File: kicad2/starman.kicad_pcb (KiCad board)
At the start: 2 copper layers, 160 x 150 mm, 104 parts, among them J1 Barrel_Jack, P1 USB_C_Plug_USB2.0, U1 ESP32-S2-MINI-1, U2 TLC5947DAP, U3 TLC5947DAP, U4 TLC5947DAP, U5 TLC5947DAP, U6 LF33_TO220, U7 LF50_TO220

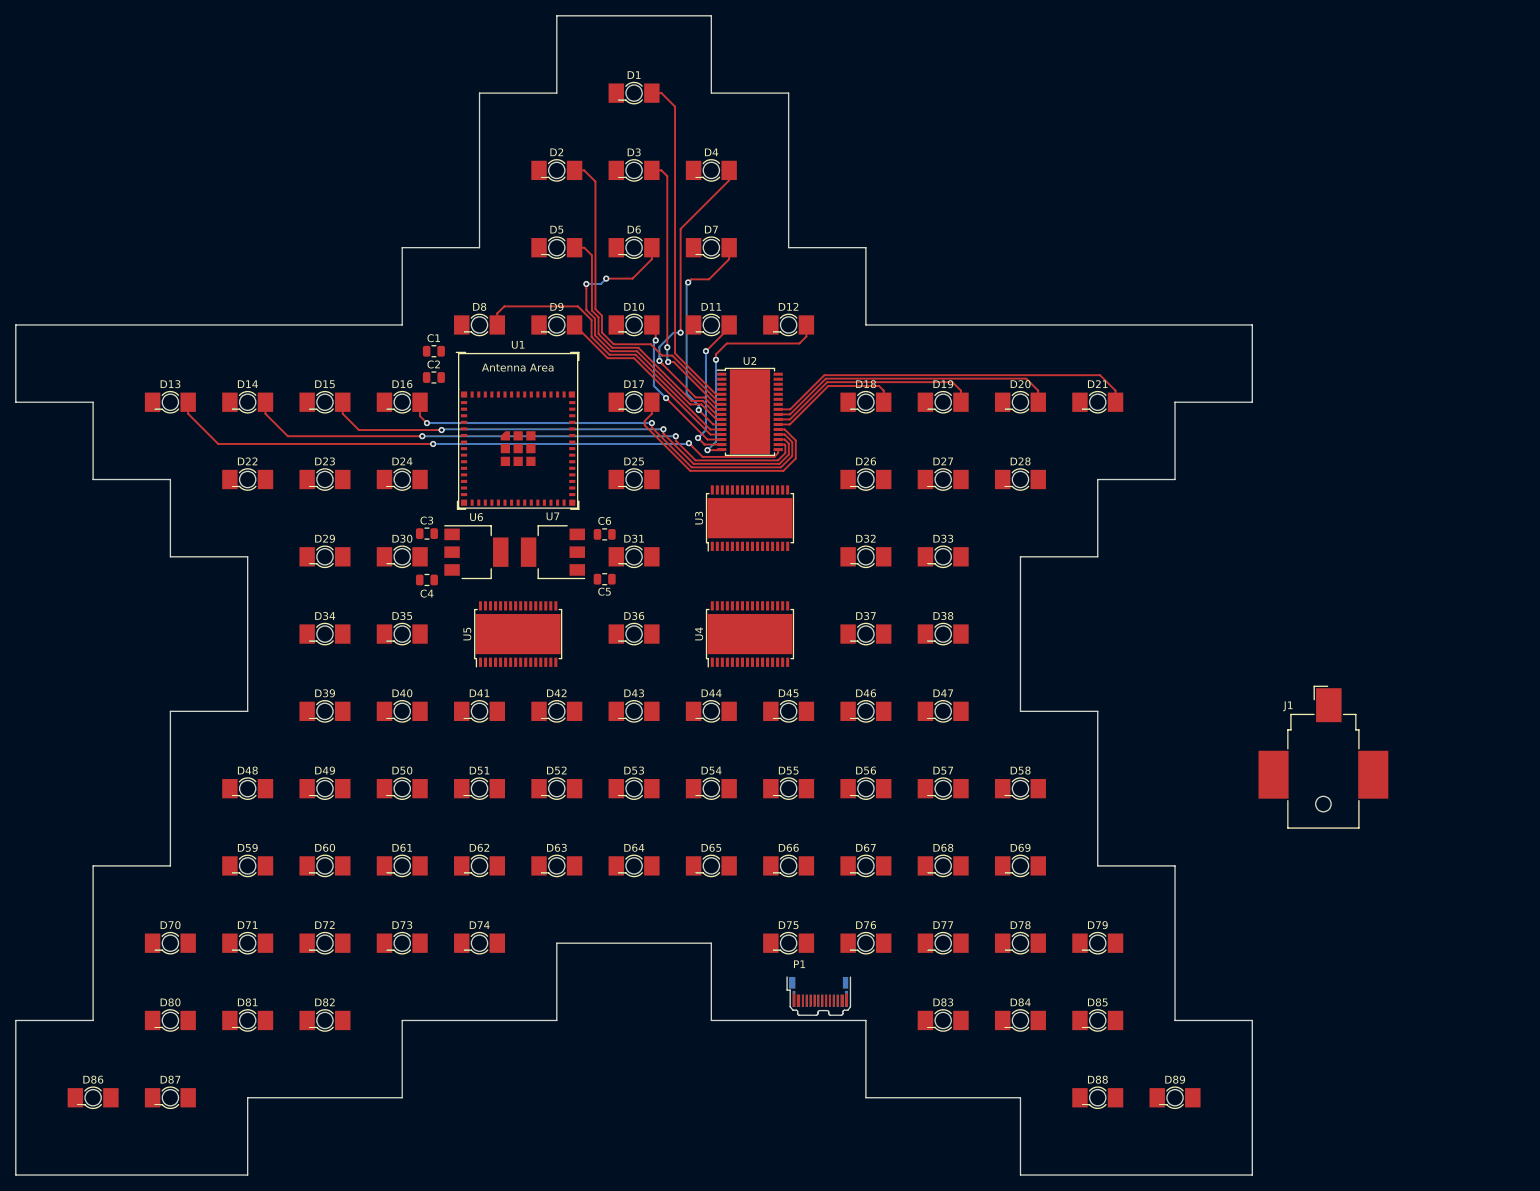
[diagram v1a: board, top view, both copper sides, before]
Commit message: Switch to PCA9959 as LED PWM driver
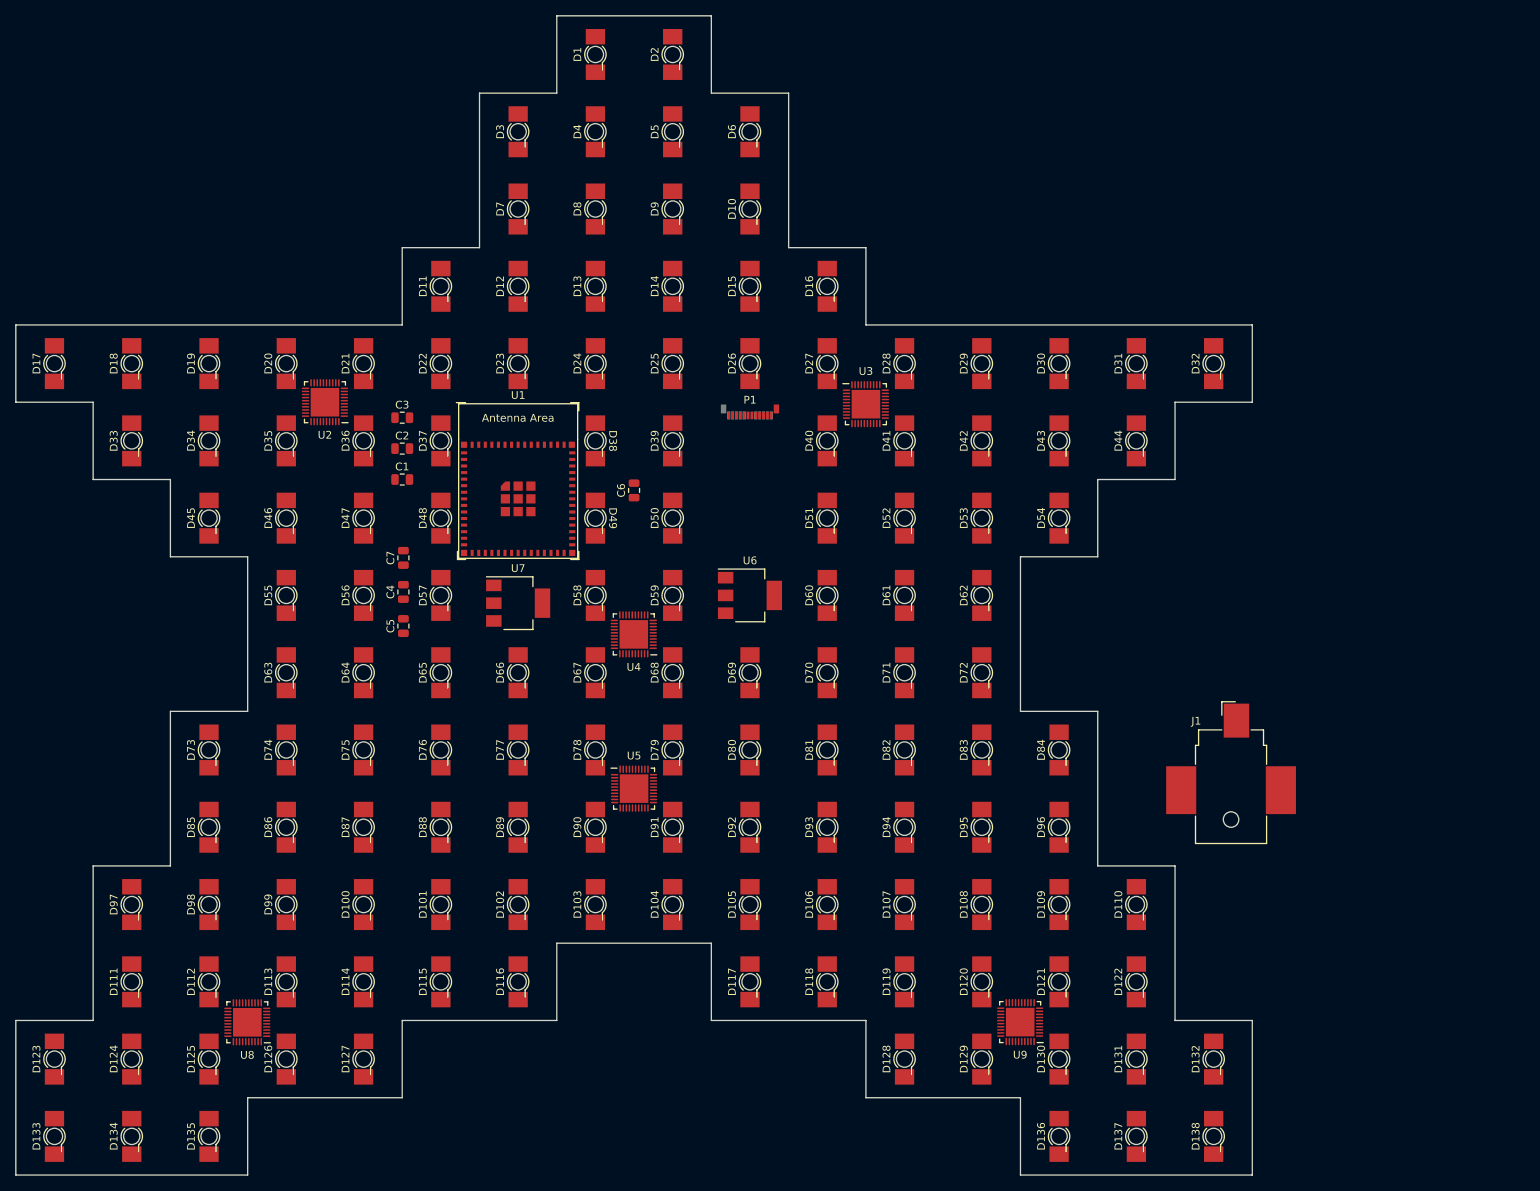
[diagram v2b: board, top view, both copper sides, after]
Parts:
- added C7: C, Capacitor_SMD:C_0805_2012Metric, F.Cu at (80.2, 100.1)
- added D100: LED, LED_SMD:LED_Osram_Lx_P47F_D2mm_ReverseMount, F.Cu at (75.0, 145.0)
- added D101: LED, LED_SMD:LED_Osram_Lx_P47F_D2mm_ReverseMount, F.Cu at (85.0, 145.0)
- added D102: LED, LED_SMD:LED_Osram_Lx_P47F_D2mm_ReverseMount, F.Cu at (95.0, 145.0)
- added D103: LED, LED_SMD:LED_Osram_Lx_P47F_D2mm_ReverseMount, F.Cu at (105.0, 145.0)
- added D104: LED, LED_SMD:LED_Osram_Lx_P47F_D2mm_ReverseMount, F.Cu at (115.0, 145.0)
- added D105: LED, LED_SMD:LED_Osram_Lx_P47F_D2mm_ReverseMount, F.Cu at (125.0, 145.0)
- added D106: LED, LED_SMD:LED_Osram_Lx_P47F_D2mm_ReverseMount, F.Cu at (135.0, 145.0)
- added D107: LED, LED_SMD:LED_Osram_Lx_P47F_D2mm_ReverseMount, F.Cu at (145.0, 145.0)
- added D108: LED, LED_SMD:LED_Osram_Lx_P47F_D2mm_ReverseMount, F.Cu at (155.0, 145.0)
- added D109: LED, LED_SMD:LED_Osram_Lx_P47F_D2mm_ReverseMount, F.Cu at (165.0, 145.0)
- added D110: LED, LED_SMD:LED_Osram_Lx_P47F_D2mm_ReverseMount, F.Cu at (175.0, 145.0)
- added D111: LED, LED_SMD:LED_Osram_Lx_P47F_D2mm_ReverseMount, F.Cu at (45.0, 155.0)
- added D112: LED, LED_SMD:LED_Osram_Lx_P47F_D2mm_ReverseMount, F.Cu at (55.0, 155.0)
- added D113: LED, LED_SMD:LED_Osram_Lx_P47F_D2mm_ReverseMount, F.Cu at (65.0, 155.0)
- added D114: LED, LED_SMD:LED_Osram_Lx_P47F_D2mm_ReverseMount, F.Cu at (75.0, 155.0)
- added D115: LED, LED_SMD:LED_Osram_Lx_P47F_D2mm_ReverseMount, F.Cu at (85.0, 155.0)
- added D116: LED, LED_SMD:LED_Osram_Lx_P47F_D2mm_ReverseMount, F.Cu at (95.0, 155.0)
- added D117: LED, LED_SMD:LED_Osram_Lx_P47F_D2mm_ReverseMount, F.Cu at (125.0, 155.0)
- added D118: LED, LED_SMD:LED_Osram_Lx_P47F_D2mm_ReverseMount, F.Cu at (135.0, 155.0)
- added D119: LED, LED_SMD:LED_Osram_Lx_P47F_D2mm_ReverseMount, F.Cu at (145.0, 155.0)
- added D120: LED, LED_SMD:LED_Osram_Lx_P47F_D2mm_ReverseMount, F.Cu at (155.0, 155.0)
- added D121: LED, LED_SMD:LED_Osram_Lx_P47F_D2mm_ReverseMount, F.Cu at (165.0, 155.0)
- added D122: LED, LED_SMD:LED_Osram_Lx_P47F_D2mm_ReverseMount, F.Cu at (175.0, 155.0)
- added D123: LED, LED_SMD:LED_Osram_Lx_P47F_D2mm_ReverseMount, F.Cu at (35.0, 165.0)
- added D124: LED, LED_SMD:LED_Osram_Lx_P47F_D2mm_ReverseMount, F.Cu at (45.0, 165.0)
- added D125: LED, LED_SMD:LED_Osram_Lx_P47F_D2mm_ReverseMount, F.Cu at (55.0, 165.0)
- added D126: LED, LED_SMD:LED_Osram_Lx_P47F_D2mm_ReverseMount, F.Cu at (65.0, 165.0)
- added D127: LED, LED_SMD:LED_Osram_Lx_P47F_D2mm_ReverseMount, F.Cu at (75.0, 165.0)
- added D128: LED, LED_SMD:LED_Osram_Lx_P47F_D2mm_ReverseMount, F.Cu at (145.0, 165.0)
- added D129: LED, LED_SMD:LED_Osram_Lx_P47F_D2mm_ReverseMount, F.Cu at (155.0, 165.0)
- added D130: LED, LED_SMD:LED_Osram_Lx_P47F_D2mm_ReverseMount, F.Cu at (165.0, 165.0)
- added D131: LED, LED_SMD:LED_Osram_Lx_P47F_D2mm_ReverseMount, F.Cu at (175.0, 165.0)
- added D132: LED, LED_SMD:LED_Osram_Lx_P47F_D2mm_ReverseMount, F.Cu at (185.0, 165.0)
- added D133: LED, LED_SMD:LED_Osram_Lx_P47F_D2mm_ReverseMount, F.Cu at (35.0, 175.0)
- added D134: LED, LED_SMD:LED_Osram_Lx_P47F_D2mm_ReverseMount, F.Cu at (45.0, 175.0)
- added D135: LED, LED_SMD:LED_Osram_Lx_P47F_D2mm_ReverseMount, F.Cu at (55.0, 175.0)
- added D136: LED, LED_SMD:LED_Osram_Lx_P47F_D2mm_ReverseMount, F.Cu at (165.0, 175.0)
- added D137: LED, LED_SMD:LED_Osram_Lx_P47F_D2mm_ReverseMount, F.Cu at (175.0, 175.0)
- added D138: LED, LED_SMD:LED_Osram_Lx_P47F_D2mm_ReverseMount, F.Cu at (185.0, 175.0)
- added D90: LED, LED_SMD:LED_Osram_Lx_P47F_D2mm_ReverseMount, F.Cu at (105.0, 135.0)
- added D91: LED, LED_SMD:LED_Osram_Lx_P47F_D2mm_ReverseMount, F.Cu at (115.0, 135.0)
- added D92: LED, LED_SMD:LED_Osram_Lx_P47F_D2mm_ReverseMount, F.Cu at (125.0, 135.0)
- added D93: LED, LED_SMD:LED_Osram_Lx_P47F_D2mm_ReverseMount, F.Cu at (135.0, 135.0)
- added D94: LED, LED_SMD:LED_Osram_Lx_P47F_D2mm_ReverseMount, F.Cu at (145.0, 135.0)
- added D95: LED, LED_SMD:LED_Osram_Lx_P47F_D2mm_ReverseMount, F.Cu at (155.0, 135.0)
- added D96: LED, LED_SMD:LED_Osram_Lx_P47F_D2mm_ReverseMount, F.Cu at (165.0, 135.0)
- added D97: LED, LED_SMD:LED_Osram_Lx_P47F_D2mm_ReverseMount, F.Cu at (45.0, 145.0)
- added D98: LED, LED_SMD:LED_Osram_Lx_P47F_D2mm_ReverseMount, F.Cu at (55.0, 145.0)
- added D99: LED, LED_SMD:LED_Osram_Lx_P47F_D2mm_ReverseMount, F.Cu at (65.0, 145.0)
- added U8: PCA9959, starman:QFN-40_EP_5x5_Pitch0.4mm, F.Cu at (60.0, 160.2)
- added U9: PCA9959, starman:QFN-40_EP_5x5_Pitch0.4mm, F.Cu at (160.0, 160.2)
- C1, C2: value C -> 10uF
- C3: value C -> 1uF
- P1: footprint Connector_USB:USB_C_Plug_JAE_DX07P024AJ1 -> Connector_USB:USB_C_Plug_Molex_105444
- U2, U3, U4, U5: value TLC5947DAP -> PCA9959; footprint Package_SO:HTSSOP-32-1EP_6.1x11mm_P0.65mm_EP5.2x11mm_Mask4.11x4.36mm -> starman:QFN-40_EP_5x5_Pitch0.4mm
- moved D85 117.7 mm to (55.0, 135.0), turned to 90 degrees
- moved D33 106.1 mm to (45.0, 85.0), turned to 90 degrees
- moved D18 95.1 mm to (45.0, 75.0), turned to 90 degrees
- moved D19 95.1 mm to (55.0, 75.0), turned to 90 degrees
- moved D20 95.1 mm to (65.0, 75.0), turned to 90 degrees
- moved D21 95.1 mm to (75.0, 75.0), turned to 90 degrees
- moved D70 91.9 mm to (135.0, 115.0), turned to 90 degrees
- moved D71 91.9 mm to (145.0, 115.0), turned to 90 degrees
- moved D72 91.9 mm to (155.0, 115.0), turned to 90 degrees
- moved D88 91.9 mm to (85.0, 135.0), turned to 90 degrees
- moved D89 91.9 mm to (95.0, 135.0), turned to 90 degrees
- moved D29 88.6 mm to (155.0, 75.0), turned to 90 degrees
- moved D30 88.6 mm to (165.0, 75.0), turned to 90 degrees
- moved D80 82.8 mm to (125.0, 125.0), turned to 90 degrees
- moved D81 82.8 mm to (135.0, 125.0), turned to 90 degrees
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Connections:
- C1 pad 1: Net-(C1-Pad1) -> GND
- C2 pad 1: Net-(C1-Pad1) -> GND
- C3 pad 2: Net-(C3-Pad2) -> +3V3
- C4 pad 2: +3V3 -> Net-(C4-Pad2)
- C5 pad 2: Net-(C3-Pad2) -> +3V3
- C6 pad 2: +5V -> Net-(C4-Pad2)
- D1 pad 1: GND -> Net-(D1-Pad1)
- D10 pad 1: GND -> Net-(D10-Pad1)
- D11 pad 1: GND -> Net-(D11-Pad1)
- D12 pad 1: GND -> Net-(D12-Pad1)
- D13 pad 1: GND -> Net-(D13-Pad1)
- D14 pad 1: GND -> Net-(D14-Pad1)
- D15 pad 1: GND -> Net-(D15-Pad1)
- D16 pad 1: GND -> Net-(D16-Pad1)
- D17 pad 1: GND -> Net-(D17-Pad1)
- D18 pad 1: GND -> Net-(D18-Pad1)
- D19 pad 1: GND -> Net-(D19-Pad1)
- D2 pad 1: GND -> Net-(D2-Pad1)
- D20 pad 1: GND -> Net-(D20-Pad1)
- D21 pad 1: GND -> Net-(D21-Pad1)
- D22 pad 1: GND -> Net-(D22-Pad1)
- D23 pad 1: GND -> Net-(D23-Pad1)
- D24 pad 1: GND -> Net-(D24-Pad1)
- D25 pad 1: GND -> Net-(D25-Pad1)
- D26 pad 1: GND -> Net-(D26-Pad1)
- D27 pad 1: GND -> Net-(D27-Pad1)
- D28 pad 1: GND -> Net-(D28-Pad1)
- D29 pad 1: GND -> Net-(D29-Pad1)
- D3 pad 1: GND -> Net-(D3-Pad1)
- D30 pad 1: GND -> Net-(D30-Pad1)
- D31 pad 1: GND -> Net-(D31-Pad1)
- D32 pad 1: GND -> Net-(D32-Pad1)
- D33 pad 1: GND -> Net-(D33-Pad1)
- D34 pad 1: GND -> Net-(D34-Pad1)
- D35 pad 1: GND -> Net-(D35-Pad1)
- D36 pad 1: GND -> Net-(D36-Pad1)
- D37 pad 1: GND -> Net-(D37-Pad1)
- D38 pad 1: GND -> Net-(D38-Pad1)
- D39 pad 1: GND -> Net-(D39-Pad1)
- D4 pad 1: GND -> Net-(D4-Pad1)
- D40 pad 1: GND -> Net-(D40-Pad1)
- D41 pad 1: GND -> Net-(D41-Pad1)
- D42 pad 1: GND -> Net-(D42-Pad1)
- D43 pad 1: GND -> Net-(D43-Pad1)
- D44 pad 1: GND -> Net-(D44-Pad1)
- D45 pad 1: GND -> Net-(D45-Pad1)
- D46 pad 1: GND -> Net-(D46-Pad1)
- D47 pad 1: GND -> Net-(D47-Pad1)
- D48 pad 1: GND -> Net-(D48-Pad1)
- D49 pad 1: GND -> Net-(D49-Pad1)
- D5 pad 1: GND -> Net-(D5-Pad1)
- D50 pad 1: GND -> Net-(D50-Pad1)
- D51 pad 1: GND -> Net-(D51-Pad1)
- D52 pad 1: GND -> Net-(D52-Pad1)
- D53 pad 1: GND -> Net-(D53-Pad1)
- D54 pad 1: GND -> Net-(D54-Pad1)
- D55 pad 1: GND -> Net-(D55-Pad1)
- D56 pad 1: GND -> Net-(D56-Pad1)
- D57 pad 1: GND -> Net-(D57-Pad1)
- D58 pad 1: GND -> Net-(D58-Pad1)
- D59 pad 1: GND -> Net-(D59-Pad1)
- D6 pad 1: GND -> Net-(D6-Pad1)
- D60 pad 1: GND -> Net-(D60-Pad1)
- D61 pad 1: GND -> Net-(D61-Pad1)
- D62 pad 1: GND -> Net-(D62-Pad1)
- D63 pad 1: GND -> Net-(D63-Pad1)
- D64 pad 1: GND -> Net-(D64-Pad1)
- D65 pad 1: GND -> Net-(D65-Pad1)
- D66 pad 1: GND -> Net-(D66-Pad1)
- D67 pad 1: GND -> Net-(D67-Pad1)
- D68 pad 1: GND -> Net-(D68-Pad1)
- D69 pad 1: GND -> Net-(D69-Pad1)
- D7 pad 1: GND -> Net-(D7-Pad1)
- D70 pad 1: GND -> Net-(D70-Pad1)
- D71 pad 1: GND -> Net-(D71-Pad1)
- D72 pad 1: GND -> Net-(D72-Pad1)
- D73 pad 1: GND -> Net-(D73-Pad1)
- D74 pad 1: GND -> Net-(D74-Pad1)
- D75 pad 1: GND -> Net-(D75-Pad1)
- D76 pad 1: GND -> Net-(D76-Pad1)
- D77 pad 1: GND -> Net-(D77-Pad1)
- D78 pad 1: GND -> Net-(D78-Pad1)
- D79 pad 1: GND -> Net-(D79-Pad1)
- D8 pad 1: GND -> Net-(D8-Pad1)
- D80 pad 1: GND -> Net-(D80-Pad1)
- D81 pad 1: GND -> Net-(D81-Pad1)
- D82 pad 1: GND -> Net-(D82-Pad1)
- D83 pad 1: GND -> Net-(D83-Pad1)
- D84 pad 1: GND -> Net-(D84-Pad1)
- D85 pad 1: GND -> Net-(D85-Pad1)
- D86 pad 1: GND -> Net-(D86-Pad1)
- D87 pad 1: GND -> Net-(D87-Pad1)
- D88 pad 1: GND -> Net-(D88-Pad1)
- D89 pad 1: GND -> Net-(D89-Pad1)
- D9 pad 1: GND -> Net-(D9-Pad1)
- J1 pad 1: Net-(C3-Pad2) -> Net-(C4-Pad2)
- P1 pad A8: (no net) -> Net-(P1-PadA8)
- P1 pad B8: (no net) -> Net-(P1-PadB8)
- U1 pad 1: Net-(C1-Pad1) -> GND
- U1 pad 2: Net-(C1-Pad1) -> GND
- U1 pad 30: Net-(C1-Pad1) -> GND
- U1 pad 42: Net-(C1-Pad1) -> GND
- U1 pad 43: Net-(C1-Pad1) -> GND
- U1 pad 46: Net-(C1-Pad1) -> GND
- U2 pad 1: GND -> Net-(U2-Pad1)
- U2 pad 10: Net-(D6-Pad2) -> Net-(U2-Pad10)
- U2 pad 11: Net-(D7-Pad2) -> Net-(U2-Pad11)
- U2 pad 12: Net-(D8-Pad2) -> Net-(U2-Pad12)
- U2 pad 13: Net-(D9-Pad2) -> Net-(D1-Pad1)
- U2 pad 14: Net-(D10-Pad2) -> Net-(D3-Pad1)
- U2 pad 15: Net-(D11-Pad2) -> Net-(D4-Pad1)
- U2 pad 16: Net-(D12-Pad2) -> Net-(D7-Pad1)
- U2 pad 17: Net-(D13-Pad2) -> Net-(D8-Pad1)
- U2 pad 18: Net-(D14-Pad2) -> Net-(D11-Pad1)
- U2 pad 19: Net-(D15-Pad2) -> Net-(D12-Pad1)
- U2 pad 2: /BLANK -> Net-(U2-Pad2)
- U2 pad 20: Net-(D16-Pad2) -> Net-(D13-Pad1)
- U2 pad 21: Net-(D17-Pad2) -> Net-(U2-Pad21)
- U2 pad 22: Net-(D18-Pad2) -> Net-(U2-Pad22)
- U2 pad 23: Net-(D19-Pad2) -> Net-(D17-Pad1)
- U2 pad 24: Net-(D20-Pad2) -> Net-(D18-Pad1)
- U2 pad 25: Net-(D21-Pad2) -> Net-(D19-Pad1)
- U2 pad 26: Net-(D22-Pad2) -> Net-(D20-Pad1)
- U2 pad 27: Net-(D23-Pad2) -> Net-(D21-Pad1)
- U2 pad 28: Net-(D24-Pad2) -> Net-(D22-Pad1)
- U2 pad 29: Net-(U2-Pad29) -> Net-(D23-Pad1)
- U2 pad 3: /SCLK -> Net-(U2-Pad3)
- U2 pad 30: /XLAT -> Net-(D33-Pad1)
- U2 pad 31: /IREF -> Net-(D34-Pad1)
- U2 pad 32: +5V -> Net-(D35-Pad1)
- U2 pad 33: GND -> Net-(D36-Pad1)
- U2 pad 4: /SIN -> Net-(U2-Pad4)
- U2 pad 5: Net-(D1-Pad2) -> Net-(U2-Pad5)
- U2 pad 6: Net-(D2-Pad2) -> Net-(U2-Pad6)
- U2 pad 7: Net-(D3-Pad2) -> Net-(U2-Pad7)
- U2 pad 8: Net-(D4-Pad2) -> Net-(U2-Pad8)
- U2 pad 9: Net-(D5-Pad2) -> Net-(U2-Pad9)
- U3 pad 1: GND -> Net-(U3-Pad1)
- U3 pad 10: Net-(D30-Pad2) -> Net-(U3-Pad10)
- U3 pad 11: Net-(D31-Pad2) -> Net-(U3-Pad11)
- U3 pad 12: Net-(D32-Pad2) -> Net-(U3-Pad12)
- U3 pad 13: Net-(D33-Pad2) -> Net-(D2-Pad1)
- U3 pad 14: Net-(D34-Pad2) -> Net-(D5-Pad1)
- U3 pad 15: Net-(D35-Pad2) -> Net-(D6-Pad1)
- U3 pad 16: Net-(D36-Pad2) -> Net-(D9-Pad1)
- U3 pad 17: Net-(D37-Pad2) -> Net-(D10-Pad1)
- U3 pad 18: Net-(D38-Pad2) -> Net-(D14-Pad1)
- U3 pad 19: Net-(D39-Pad2) -> Net-(D15-Pad1)
- U3 pad 2: /BLANK -> Net-(U3-Pad2)
- U3 pad 20: Net-(D40-Pad2) -> Net-(D16-Pad1)
- U3 pad 21: Net-(D41-Pad2) -> Net-(U3-Pad21)
- U3 pad 22: Net-(D42-Pad2) -> Net-(U3-Pad22)
- U3 pad 23: Net-(D43-Pad2) -> Net-(D24-Pad1)
- U3 pad 24: Net-(D44-Pad2) -> Net-(D25-Pad1)
- U3 pad 25: Net-(D45-Pad2) -> Net-(D26-Pad1)
- U3 pad 26: Net-(D46-Pad2) -> Net-(D27-Pad1)
- U3 pad 27: Net-(D47-Pad2) -> Net-(D28-Pad1)
- U3 pad 28: Net-(D48-Pad2) -> Net-(D29-Pad1)
- U3 pad 29: Net-(U3-Pad29) -> Net-(D30-Pad1)
- U3 pad 3: /SCLK -> Net-(U3-Pad3)
- U3 pad 30: /XLAT -> Net-(D31-Pad1)
- U3 pad 31: /IREF -> Net-(D32-Pad1)
- U3 pad 32: +5V -> Net-(D38-Pad1)
- U3 pad 33: GND -> Net-(D39-Pad1)
- U3 pad 5: Net-(D25-Pad2) -> Net-(U3-Pad5)
- U3 pad 6: Net-(D26-Pad2) -> Net-(U3-Pad6)
- U3 pad 7: Net-(D27-Pad2) -> Net-(U3-Pad7)
- U3 pad 8: Net-(D28-Pad2) -> Net-(U3-Pad8)
- U3 pad 9: Net-(D29-Pad2) -> Net-(U3-Pad9)
- U4 pad 1: GND -> Net-(U4-Pad1)
- U4 pad 10: Net-(D54-Pad2) -> Net-(U4-Pad10)
- U4 pad 11: Net-(D55-Pad2) -> Net-(U4-Pad11)
- U4 pad 12: Net-(D56-Pad2) -> Net-(U4-Pad12)
- U4 pad 13: Net-(D57-Pad2) -> Net-(D49-Pad1)
- U4 pad 14: Net-(D58-Pad2) -> Net-(D50-Pad1)
- U4 pad 15: Net-(D59-Pad2) -> Net-(D51-Pad1)
- U4 pad 16: Net-(D60-Pad2) -> Net-(D52-Pad1)
- U4 pad 17: Net-(D61-Pad2) -> Net-(D53-Pad1)
- U4 pad 18: Net-(D62-Pad2) -> Net-(D54-Pad1)
- U4 pad 19: Net-(D63-Pad2) -> Net-(D55-Pad1)
- U4 pad 2: /BLANK -> Net-(U4-Pad2)
- U4 pad 20: Net-(D64-Pad2) -> Net-(D56-Pad1)
- U4 pad 21: Net-(D65-Pad2) -> Net-(U4-Pad21)
- U4 pad 22: Net-(D66-Pad2) -> Net-(U4-Pad22)
- U4 pad 23: Net-(D67-Pad2) -> Net-(D57-Pad1)
- U4 pad 24: Net-(D68-Pad2) -> Net-(D58-Pad1)
- U4 pad 25: Net-(D69-Pad2) -> Net-(D59-Pad1)
- U4 pad 26: Net-(D70-Pad2) -> Net-(D60-Pad1)
- U4 pad 27: Net-(D71-Pad2) -> Net-(D61-Pad1)
- U4 pad 28: Net-(D72-Pad2) -> Net-(D62-Pad1)
- U4 pad 29: Net-(U3-Pad4) -> Net-(D63-Pad1)
- U4 pad 3: /SCLK -> Net-(U4-Pad3)
- U4 pad 30: /XLAT -> Net-(D64-Pad1)
- U4 pad 31: /IREF -> Net-(D65-Pad1)
- U4 pad 32: +5V -> Net-(D66-Pad1)
- U4 pad 33: GND -> Net-(D67-Pad1)
- U4 pad 4: Net-(U2-Pad29) -> Net-(U4-Pad4)
- U4 pad 5: Net-(D49-Pad2) -> Net-(U4-Pad5)
- U4 pad 6: Net-(D50-Pad2) -> Net-(U4-Pad6)
- U4 pad 7: Net-(D51-Pad2) -> Net-(U4-Pad7)
- U4 pad 8: Net-(D52-Pad2) -> Net-(U4-Pad8)
- U4 pad 9: Net-(D53-Pad2) -> Net-(U4-Pad9)
- U5 pad 1: GND -> Net-(U5-Pad1)
- U5 pad 10: Net-(D78-Pad2) -> Net-(U5-Pad10)
- U5 pad 11: Net-(D79-Pad2) -> Net-(U5-Pad11)
- U5 pad 12: Net-(D80-Pad2) -> Net-(U5-Pad12)
- U5 pad 13: Net-(D81-Pad2) -> Net-(D73-Pad1)
- U5 pad 14: Net-(D82-Pad2) -> Net-(D74-Pad1)
- U5 pad 15: Net-(D83-Pad2) -> Net-(D75-Pad1)
- U5 pad 16: Net-(D84-Pad2) -> Net-(D76-Pad1)
- U5 pad 17: Net-(D85-Pad2) -> Net-(D77-Pad1)
- U5 pad 18: Net-(D86-Pad2) -> Net-(D78-Pad1)
- U5 pad 19: Net-(D87-Pad2) -> Net-(D79-Pad1)
- U5 pad 2: /BLANK -> Net-(U5-Pad2)
- U5 pad 20: Net-(D88-Pad2) -> Net-(D80-Pad1)
- U5 pad 21: Net-(D89-Pad2) -> Net-(U5-Pad21)
- U5 pad 23: Net-(U5-Pad23) -> Net-(D81-Pad1)
- U5 pad 24: Net-(U5-Pad24) -> Net-(D82-Pad1)
- U5 pad 25: Net-(U5-Pad25) -> Net-(D83-Pad1)
- U5 pad 26: Net-(U5-Pad26) -> Net-(D84-Pad1)
- U5 pad 27: Net-(U5-Pad27) -> Net-(D85-Pad1)
- U5 pad 28: Net-(U5-Pad28) -> Net-(D86-Pad1)
- U5 pad 29: Net-(U5-Pad29) -> Net-(D87-Pad1)
- U5 pad 3: /SCLK -> Net-(U5-Pad3)
- U5 pad 30: /XLAT -> Net-(D88-Pad1)
- U5 pad 31: /IREF -> Net-(D89-Pad1)
- U5 pad 32: +5V -> Net-(D90-Pad1)
- U5 pad 33: GND -> Net-(D91-Pad1)
- U5 pad 4: Net-(U3-Pad29) -> Net-(U5-Pad4)
- U5 pad 5: Net-(D73-Pad2) -> Net-(U5-Pad5)
- U5 pad 6: Net-(D74-Pad2) -> Net-(U5-Pad6)
- U5 pad 7: Net-(D75-Pad2) -> Net-(U5-Pad7)
- U5 pad 8: Net-(D76-Pad2) -> Net-(U5-Pad8)
- U5 pad 9: Net-(D77-Pad2) -> Net-(U5-Pad9)
- U6 pad 1: Net-(C3-Pad2) -> Net-(C4-Pad2)
- U7 pad 1: Net-(C3-Pad2) -> Net-(C4-Pad2)
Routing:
- net Net-(D13-Pad2): track 80.9 -> 0.00 mm, vias 2 -> 0
- net Net-(D14-Pad2): track 74.0 -> 0.00 mm, vias 2 -> 0
- net Net-(D15-Pad2): track 65.8 -> 0.00 mm, vias 2 -> 0
- net Net-(D16-Pad2): track 57.7 -> 0.00 mm, vias 2 -> 0
- net Net-(D21-Pad2): track 47.8 -> 0.00 mm
- net Net-(D1-Pad2): track 43.9 -> 0.00 mm
- net Net-(D2-Pad2): track 42.3 -> 0.00 mm
- net Net-(D4-Pad2): track 39.6 -> 0.00 mm, vias 2 -> 0
- net Net-(D6-Pad2): track 39.3 -> 0.00 mm, vias 2 -> 0
- net Net-(D8-Pad2): track 38.8 -> 0.00 mm
- net Net-(D20-Pad2): track 37.7 -> 0.00 mm
- net Net-(D3-Pad2): track 35.6 -> 0.00 mm, vias 2 -> 0
- net Net-(D5-Pad2): track 33.4 -> 0.00 mm
- net Net-(D17-Pad2): track 31.2 -> 0.00 mm
- net Net-(D7-Pad2): track 29.0 -> 0.00 mm, vias 2 -> 0
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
